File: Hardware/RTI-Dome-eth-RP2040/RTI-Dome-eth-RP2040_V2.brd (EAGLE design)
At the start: 111.1 x 76.3 mm, 107 parts, among them IC2 24LC64T-I/SN, IC3 FT232RL, IC4 RASPBERRY_PI_PICO, IC8 REG1117-3.3V, IC9 REG1117-5V, J2 XT60PW-M, U1 W5500, X13 PN61729-S, X9 J1011F21PNL

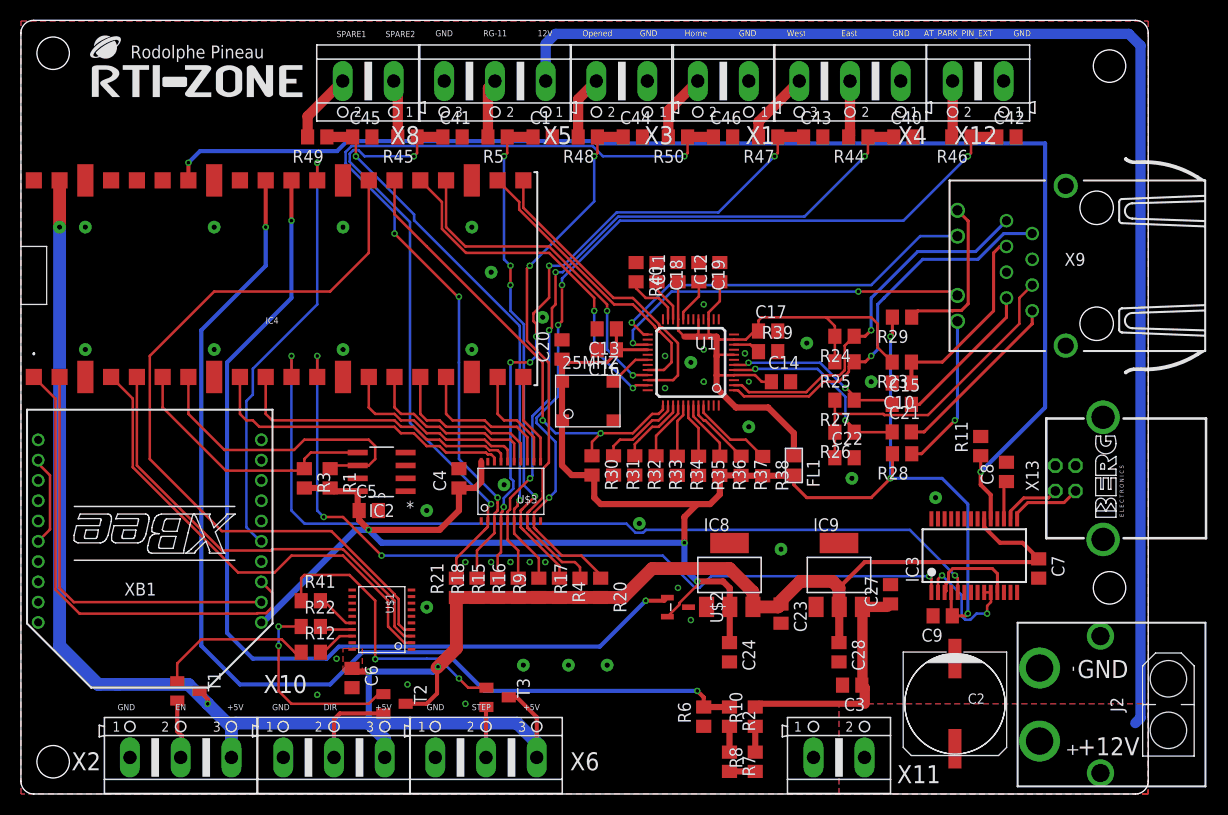
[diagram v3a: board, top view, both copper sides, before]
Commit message: New RP2040 shutter board
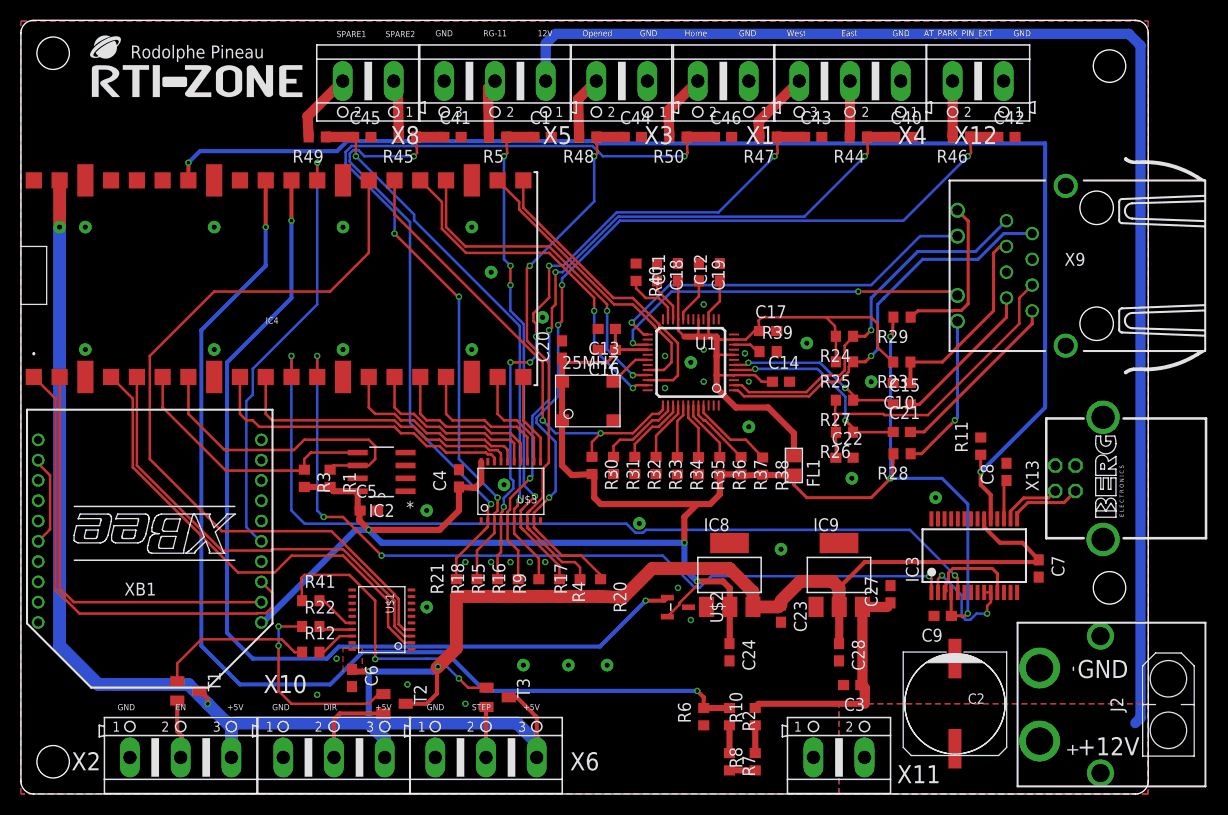
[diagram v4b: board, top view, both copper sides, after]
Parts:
- C1, C10, C11, C12, C13, C14, C15, C16, C17, C18, C19, C20, C21, C22, C23, C24, C27, C28, C3, C4, C40, C41, C42, C43, C44, C45, C46, C5, C6, C7, C8, C9: device rcl:C0805 -> rcl:C0603
- R1, R10, R11, R12, R15, R16, R17, R18, R2, R20, R21, R22, R23, R24, R25, R26, R27, R28, R29, R3, R30, R31, R32, R33, R34, R35, R36, R37, R38, R39, R4, R40, R41, R44, R45, R46, R47, R48, R49, R5, R50, R6, R7, R8, R9: device rcl:R0805 -> rcl:R0603
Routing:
- net 3.3V: track 197.7 -> 198.7 mm

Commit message: Fix some components
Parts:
- removed U$2: MCP120T, MCP120T:SOT95P237X112-3N
- T1, T2, T3: value (none) -> MMBT3904LT1; device transistor:SOT23-BEC -> samacsys:SOT23
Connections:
- net 3.3V: no longer U$2.2
- net DIR-5V_TR: now also T2.1; no longer T2.B
- net DIR_5V_OUT: now also T2.2; no longer T2.E
- net EN-5V_TR: now also T1.1; no longer T1.B
- net EN_5V_OUT: now also T1.2; no longer T1.E
- net GND: no longer U$2.3
- net RESET: no longer U$2.1
- net STEP-5V_TR: now also T3.1; no longer T3.B
- net STEP_5V_OUT: now also T3.2; no longer T3.E
- net VCC: now also T1.3, T2.3, T3.3; no longer T1.C, T2.C, T3.C
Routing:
- net RESET: track 94.2 -> 0.00 mm, vias 2 -> 0
- net 3.3V: track 198.7 -> 194.0 mm
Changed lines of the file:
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@@
 <attribute name="VALUE" x="57.56275" y="30.48" size="1.27" layer="27" rot="R270"/>
-</element>
-<element name="U$2" library="MCP120T" library_urn="urn:adsk.eagle:library:38117017" package="SOT95P237X112-3N" package3d_urn="urn:adsk.eagle:package:38117020/3" value="MCP120T" x="64.77" y="18.415" smashed="yes" rot="R270">
-<attribute name="DESCRIPTION" value="Microcontroller Supervisory Circuit" x="74.93" y="31.115" size="1.778" layer="27" rot="R270" display="off"/>
-<attribute name="HEIGHT" value="mm" x="74.93" y="31.115" size="1.778" layer="27" rot="R270" display="off"/>
-<attribute name="MANUFACTURER_NAME" value="Microchip" x="74.93" y="31.115" size="1.778" layer="27" rot="R270" display="off"/>
-<attribute name="MANUFACTURER_PART_NUMBER" value="MCP120T-315I/TT" x="74.93" y="31.115" size="1.778" layer="27" rot="R270" display="off"/>
-<attribute name="MOUSER_PART_NUMBER" value="579-MCP120T-315I/TT" x="74.93" y="31.115" size="1.778" layer="27" rot="R270" display="off"/>
-<attribute name="MOUSER_PRICE-STOCK" value="https://www.mouser.com/ProductDetail/Microchip-Technology/MCP120T-315I-TT/?qs=6pREnGtJ7gEI3DoW5cf%2FYQ%3D%3D" x="74.93" y="31.115" size="1.778" layer="27" rot="R270" display="off"/>
-<attribute name="MPN" value="MCP120T-270I/TT" x="64.77" y="18.415" size="1.778" layer="27" rot="R270" display="off"/>
-<attribute name="NAME" x="68.58" y="18.415" size="1.27" layer="25" rot="R270" align="center"/>
-<attribute name="VALUE" x="60.96" y="18.415" size="1.27" layer="27" rot="R270" align="center"/>
 </element>
 <element name="C13" library="rcl" library_urn="urn:adsk.eagle:library:334" package="C0603" package3d_urn="urn:adsk.eagle:package:23616/2" value="10nF" x="57.75325" y="45.847" smashed="yes" rot="R180">
@@
 <attribute name="VALUE" x="50.915" y="31.365" size="0.8128" layer="27" font="vector" rot="R180"/>
 </element>
-<element name="T1" library="transistor" library_urn="urn:adsk.eagle:library:402" package="SOT23-BEC" package3d_urn="urn:adsk.eagle:package:28748/2" value="" x="16.51" y="10.16" smashed="yes" rot="R270">
+<element name="T1" library="samacsys" library_urn="urn:adsk.eagle:library:37256869" package="SOT23" package3d_urn="urn:adsk.eagle:package:28738/2" value="MMBT3904LT1" x="16.51" y="10.16" smashed="yes" rot="R270">
 <attribute name="NAME" x="18.415" y="12.065" size="1.27" layer="25" rot="R270"/>
-<attribute name="POPULARITY" value="0" x="16.51" y="10.16" size="1.778" layer="27" rot="R270" display="off"/>
+<attribute name="POPULARITY" value="13" x="16.51" y="10.16" size="1.778" layer="27" rot="R270" display="off"/>
 <attribute name="VALUE" x="13.335" y="12.065" size="1.27" layer="27" rot="R270"/>
 </element>
-<element name="T2" library="transistor" library_urn="urn:adsk.eagle:library:402" package="SOT23-BEC" package3d_urn="urn:adsk.eagle:package:28748/2" value="" x="36.83" y="8.89" smashed="yes" rot="R270">
+<element name="T2" library="samacsys" library_urn="urn:adsk.eagle:library:37256869" package="SOT23" package3d_urn="urn:adsk.eagle:package:28738/2" value="MMBT3904LT1" x="36.83" y="8.89" smashed="yes" rot="R270">
 <attribute name="NAME" x="38.735" y="10.795" size="1.27" layer="25" rot="R270"/>
-<attribute name="POPULARITY" value="0" x="36.83" y="8.89" size="1.778" layer="27" rot="R270" display="off"/>
+<attribute name="POPULARITY" value="13" x="36.83" y="8.89" size="1.778" layer="27" rot="R270" display="off"/>
 <attribute name="VALUE" x="33.655" y="10.795" size="1.27" layer="27" rot="R270"/>
 </element>
-<element name="T3" library="transistor" library_urn="urn:adsk.eagle:library:402" package="SOT23-BEC" package3d_urn="urn:adsk.eagle:package:28748/2" value="" x="46.99" y="9.525" smashed="yes" rot="R270">
+<element name="T3" library="samacsys" library_urn="urn:adsk.eagle:library:37256869" package="SOT23" package3d_urn="urn:adsk.eagle:package:28738/2" value="MMBT3904LT1" x="46.99" y="9.525" smashed="yes" rot="R270">
 <attribute name="NAME" x="48.895" y="11.43" size="1.27" layer="25" rot="R270"/>
-<attribute name="POPULARITY" value="0" x="46.99" y="9.525" size="1.778" layer="27" rot="R270" display="off"/>
+<attribute name="POPULARITY" value="13" x="46.99" y="9.525" size="1.778" layer="27" rot="R270" display="off"/>
 <attribute name="VALUE" x="43.815" y="11.43" size="1.27" layer="27" rot="R270"/>
 </element>
@@
 <contactref element="25MHZ" pad="2"/>
 <contactref element="C20" pad="2"/>
-<contactref element="U$2" pad="3"/>
 <contactref element="C16" pad="2"/>
 <contactref element="C13" pad="2"/>
@@
 <contactref element="R1" pad="2"/>
 <contactref element="C5" pad="1"/>
-<contactref element="U$2" pad="2"/>
 <contactref element="IC2" pad="8"/>
 <contactref element="IC8" pad="2"/>
@@
 <wire x1="86.015" y1="33.54" x2="85.915" y2="31.305" width="0.3048" layer="1"/>
 <wire x1="85.915" y1="31.305" x2="85.725" y2="31.115" width="0.3048" layer="1"/>
-<wire x1="63.7286" y1="17.4752" x2="64.897" y2="18.6436" width="0.254" layer="1"/>
-<wire x1="64.897" y1="18.6436" x2="64.897" y2="18.81013125" width="0.254" layer="1"/>
-<wire x1="66.675" y1="20.58813125" x2="66.675" y2="20.955" width="0.254" layer="1"/>
-<wire x1="64.897" y1="18.81013125" x2="66.675" y2="20.58813125" width="0.254" layer="1"/>
 <wire x1="77.47" y1="29.21" x2="76.2" y2="30.48" width="0.3048" layer="1"/>
 <wire x1="76.2" y1="30.48" x2="76.2" y2="31.435" width="0.3048" layer="1"/>
@@
 <wire x1="32.639" y1="12.28" x2="32.954" y2="12.065" width="0.4064" layer="1"/>
 <wire x1="32.954" y1="12.065" x2="34.29" y2="12.065" width="0.6096" layer="1"/>
-<contactref element="T1" pad="C"/>
-<contactref element="T2" pad="C"/>
+<contactref element="T1" pad="3"/>
+<contactref element="T2" pad="3"/>
 <wire x1="17.61" y1="10.16" x2="18.415" y2="9.355" width="0.4064" layer="1"/>
 <wire x1="18.415" y1="9.355" x2="18.415" y2="8.89" width="0.4064" layer="1"/>
 <via x="18.415" y="8.89" extent="1-16" drill="0.35"/>
-<contactref element="T3" pad="C"/>
+<contactref element="T3" pad="3"/>
 <wire x1="37.93" y1="8.89" x2="40.005" y2="8.89" width="0.4064" layer="1"/>
 <wire x1="40.005" y1="8.89" x2="41.021" y2="9.906" width="0.4064" layer="1"/>
@@
 </signal>
 <signal name="RESET">
-<contactref element="U$2" pad="1"/>
 <contactref element="IC4" pad="30"/>
-<wire x1="26.67" y1="60.49" x2="26.67" y2="56.515" width="0.4064" layer="1"/>
-<via x="26.67" y="56.515" extent="1-16" drill="0.35"/>
-<wire x1="26.67" y1="56.515" x2="26.67" y2="48.895" width="0.4064" layer="16"/>
-<wire x1="26.67" y1="48.895" x2="20.32" y2="42.545" width="0.4064" layer="16"/>
-<wire x1="20.32" y1="42.545" x2="20.32" y2="15.875" width="0.4064" layer="16"/>
-<wire x1="20.32" y1="15.875" x2="22.86" y2="13.335" width="0.4064" layer="16"/>
-<wire x1="22.86" y1="13.335" x2="30.1490875" y2="13.335" width="0.4064" layer="16"/>
-<wire x1="30.1490875" y1="13.335" x2="31.3428875" y2="14.5288" width="0.4064" layer="16"/>
-<wire x1="57.0738" y1="14.5288" x2="61.595" y2="19.05" width="0.4064" layer="16"/>
-<wire x1="31.3428875" y1="14.5288" x2="57.0738" y2="14.5288" width="0.4064" layer="16"/>
-<via x="61.595" y="19.05" extent="1-16" drill="0.35"/>
-<wire x1="61.595" y1="19.05" x2="63.4238" y2="19.05" width="0.4064" layer="1"/>
-<wire x1="63.4238" y1="19.05" x2="63.7286" y2="19.3548" width="0.4064" layer="1"/>
 </signal>
 <signal name="AVDD">
@@
 <signal name="DIR-5V_TR">
 <contactref element="R22" pad="1"/>
-<contactref element="T2" pad="B"/>
+<contactref element="T2" pad="1"/>
 <wire x1="27.725" y1="16.51" x2="25.4" y2="16.51" width="0.254" layer="1"/>
 <via x="25.4" y="16.51" extent="1-16" drill="0.35"/>
@@
 <signal name="STEP-5V_TR">
 <contactref element="R41" pad="1"/>
-<contactref element="T3" pad="B"/>
+<contactref element="T3" pad="1"/>
 <wire x1="27.725" y1="19.05" x2="27.625" y2="21.275" width="0.254" layer="1"/>
 <wire x1="27.625" y1="21.275" x2="27.94" y2="21.59" width="0.254" layer="1"/>
@@
 <signal name="EN-5V_TR">
 <contactref element="R12" pad="1"/>
-<contactref element="T1" pad="B"/>
+<contactref element="T1" pad="1"/>
 <wire x1="15.41" y1="12.87" x2="15.41" y2="11.11" width="0.254" layer="1"/>
 <wire x1="27.725" y1="13.97" x2="26.99" y2="13.97" width="0.254" layer="1"/>
@@
 </signal>
 <signal name="EN_5V_OUT">
-<contactref element="T1" pad="E"/>
+<contactref element="T1" pad="2"/>
 <contactref element="X2" pad="2"/>
 <wire x1="15.41" y1="9.21" x2="15.41" y2="6.18" width="0.4064" layer="1"/>
@@
 </signal>
 <signal name="DIR_5V_OUT">
-<contactref element="T2" pad="E"/>
+<contactref element="T2" pad="2"/>
 <contactref element="X10" pad="2"/>
 <wire x1="35.73" y1="7.94" x2="31.435" y2="7.94" width="0.4064" layer="1"/>
@@
 </signal>
 <signal name="STEP_5V_OUT">
-<contactref element="T3" pad="E"/>
+<contactref element="T3" pad="2"/>
 <contactref element="X6" pad="2"/>
 <wire x1="45.89" y1="8.575" x2="45.847" y2="8.532" width="0.4064" layer="1"/>

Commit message: Soem minor fixes on the PCB
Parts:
- X9: value J1011F21PNL -> J1011F01PNL; device rti:J1011F21PNL -> rti:J1011F01PNL

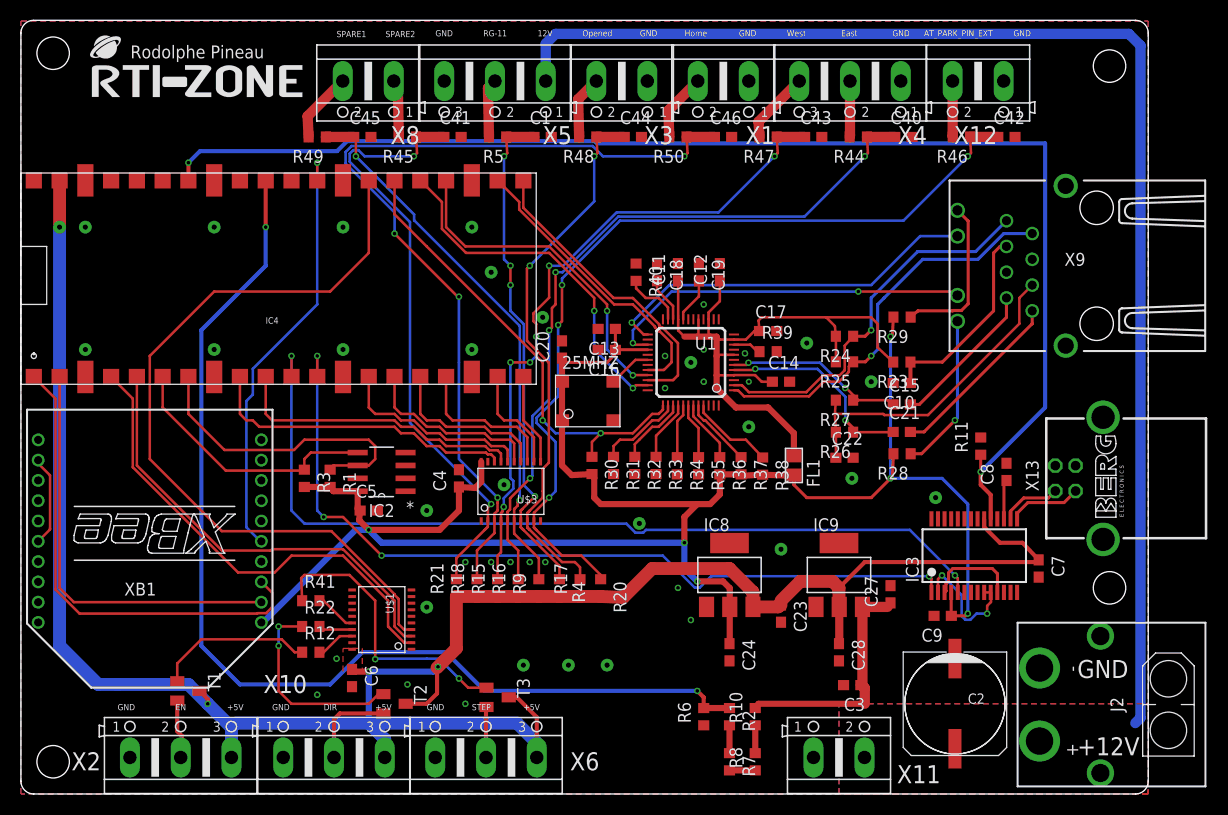
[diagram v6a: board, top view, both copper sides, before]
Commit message: Change 5V regulator for 1A version
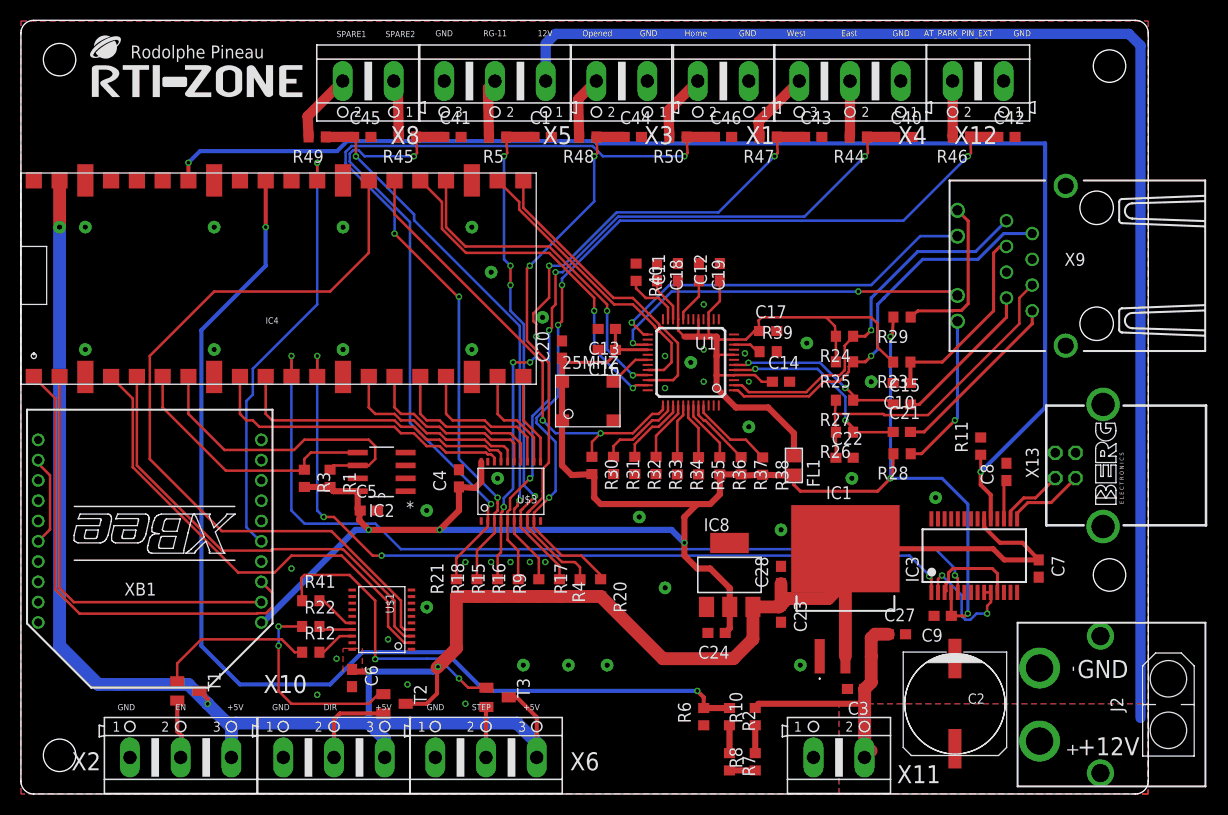
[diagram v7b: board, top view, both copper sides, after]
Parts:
- removed IC9: REG1117-5V, burr-brown:SOT223
- added IC1: REG1117FA-5.0_500, REG1117FA-5.0_500:REG1117FA50500
- moved C28 9.52 mm to (74.9, 21.6), turned to 90 degrees
- moved C27 3.99 mm to (86.4, 15.7), turned to 0 degrees
- moved C24 2.29 mm to (68.6, 15.9), turned to 180 degrees
- moved X13 1.27 mm to (106.7, 32.4)
- moved C3 0.54 mm to (82.3, 10.4)
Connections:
- net +12V: now also IC1.3; no longer IC9.3
- net GND: now also IC1.1; no longer IC9.1
- net VCC: now also IC1.2, IC1.4; no longer IC9.2
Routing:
- net VCC: track 219.4 -> 231.6 mm
- net 3.3V: track 194.0 -> 184.8 mm
- net +12V: track 154.3 -> 155.3 mm
- net RX2: track 82.9 -> 82.1 mm
- net USBD_P: track 7.22 -> 7.75 mm
- net USBD_N: track 6.00 -> 6.53 mm
